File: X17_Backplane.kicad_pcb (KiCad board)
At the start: 2 copper layers, 89.2 x 110 mm, 30 parts, among them J1 430450212, J10 Conn_01x01, J11 Conn_01x01, J13 Conn_01x01, J14 ET60S-D04-3-08-D04-X-R1-S, J15 Conn_01x01, J16 Conn_01x01, J18 430450212, J19 DF11-10DS-2DSA05, J2 IPS1-105-01-L-D, J3 IPS1-105-01-L-D, J4 Conn_01x02_Pin, J5 Conn_01x04_Pin, J6 Conn_01x01, J7 Conn_01x01, J8 430450612, J9 Conn_01x01, U1 282837-4, U2 ULN2003AD, U3 SolenoidConn

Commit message: Work done on11/17/2024
I'm cooked yo
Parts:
- U1: value 282837-4 -> 282837-6; footprint TB_282837_4:282837-4_TYC -> 282837_6:282837-6_TYC
- moved J18 144.6 mm to (119.2, 146.5)
- moved J1 101.7 mm to (132.2, 146.5)
- moved U1 100.0 mm to (151.3, 145.8)
- moved J8 29.0 mm to (105.8, 146.5)
- moved J19 5.30 mm to (149.7, 131.8)
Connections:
- net A renamed A+
- net A_TB renamed A_TB+
- net B renamed A-
- J1 pad 1: B_TB -> A_TB-
- J14 pad 03: NRST2 -> NRST_PSB
- J14 pad 05: unconnected-(J14-Pad05) -> 48V
- J14 pad 06: unconnected-(J14-Pad06) -> 48V
- J14 pad 07: unconnected-(J14-Pad07) -> 48V_GND
- J14 pad 08: unconnected-(J14-Pad08) -> 48V_GND
- J14 pad P05_1: 48V_GND -> P05_7
- J14 pad P06_1: 48V_GND -> P06_6
- J14 pad P07_1: 48V -> P07_8
- J14 pad P08_1: 48V -> P08_6
- J19 pad 16: NRST -> NRST_ESCC
- J8 pad 3: 5V_TB -> NRST_PSB
- J8 pad 4: 5V_GNDTB -> NRST_ESCC
- J8 pad 5: NRST2 -> NRST_TB
- J8 pad 6: NRST -> 5V_GNDTB
- U1 pad 1: 48V -> 48V_GND
- U1 pad 2: 48V_GND -> 48V
- U1 pad 3: B_TB -> NRST_TB
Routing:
- net 12V_GND1: track 0.00 -> 153.8 mm, vias 0 -> 2
- net 12V_GND2: track 0.00 -> 130.9 mm, vias 0 -> 2
- net 5V: track 0.00 -> 130.5 mm
- net 48V: track 0.00 -> 72.6 mm
- net 48V_GND: track 0.00 -> 65.4 mm
- net A_TB+: track 0.00 -> 40.0 mm
- net A_TB-: track 0.00 -> 40.0 mm
- net A-: track 0.00 -> 36.9 mm, vias 0 -> 2
- net A+: track 0.00 -> 36.3 mm, vias 0 -> 2
- net 12V_1: track 0.00 -> 33.0 mm
- net 5V_GND: track 0.00 -> 21.4 mm, vias 0 -> 5
- net PWMB3: track 0.00 -> 11.6 mm
- net PWMB2: track 0.00 -> 9.69 mm
- net PWMB1: track 0.00 -> 8.95 mm
- net PWMB0: track 0.00 -> 8.68 mm
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- added copper zone on B.Cu, net 12V_1
- added copper zone on B.Cu, net 12V_2
- added copper zone on B.Cu, net 12V_GND1
- added copper zone on B.Cu, net 12V_GND2
- added copper zone on B.Cu, net 5V_GND
- removed copper zone on F.Cu, net 12V_1
- removed copper zone on F.Cu, net 12V_2
- removed copper zone on F.Cu, net 12V_GND1
- removed copper zone on F.Cu, net 12V_GND2

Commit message: WORK done on 11/20/2024
I'm losing my shiiiiiii
#SlayedTheDayAway
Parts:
- added R8: 4K, Resistor_SMD:R_0805_2012Metric, F.Cu at (264.2, 100.0)
- moved R6 131.1 mm to (126.8, 107.0), turned to -90 degrees
- moved R8 127.4 mm to (130.5, 128.2)
- moved D2 127.2 mm to (126.8, 102.0), turned to 90 degrees
- moved D4 126.0 mm to (127.2, 124.5)
- moved R5 111.6 mm to (151.5, 77.4), turned to -90 degrees
- moved D1 108.8 mm to (151.5, 73.2), turned to 90 degrees
- moved R7 94.7 mm to (168.5, 85.8), turned to -90 degrees
- moved D3 92.6 mm to (168.5, 80.8), turned to 90 degrees
- moved C2 64.0 mm to (192.2, 104.8), turned to -90 degrees
- moved U3 50.9 mm to (167.8, 62.0), turned to 90 degrees
- moved U2 31.7 mm to (154.9, 51.6), turned to 0 degrees
- moved J19 2.30 mm to (149.2, 129.5)
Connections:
- J19 pad 3: A+ -> PWMA1
- J19 pad 4: A- -> A+
- J19 pad 6: PWMA1 -> A-
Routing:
- net NRST_ESCC: track 0.00 -> 102.2 mm, vias 0 -> 6
- net NRST_PSB: track 0.00 -> 91.9 mm, vias 0 -> 4
- net 5V_GNDTB: track 0.00 -> 90.6 mm, vias 0 -> 8
- net 12V_2: track 0.00 -> 77.7 mm, vias 0 -> 14
- net A-: track 36.9 -> 114.0 mm, vias 2 -> 6
- net 12V_1: track 33.0 -> 110.1 mm, vias 0 -> 11
- net A+: track 36.3 -> 112.6 mm, vias 2 -> 4
- net PWMA3: track 0.00 -> 74.6 mm, vias 0 -> 2
- net NRST_TB: track 0.00 -> 74.5 mm, vias 0 -> 6
- net PWMA0: track 0.16 -> 70.8 mm
- net PWMA1: track 0.00 -> 64.5 mm
- net PWMA2: track 0.00 -> 60.4 mm, vias 0 -> 2
- net Telemetry: track 0.00 -> 58.7 mm, vias 0 -> 2
- net PWMB1: track 8.95 -> 59.3 mm, vias 0 -> 4
- net 12V_GND2: track 130.9 -> 88.2 mm, vias 2 -> 16
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- added copper zone on F.Cu, net 12V_1
- added copper zone on F.Cu, net 12V_2
- added copper zone on F.Cu, net 12V_GND1
- added copper zone on F.Cu, net 12V_GND2

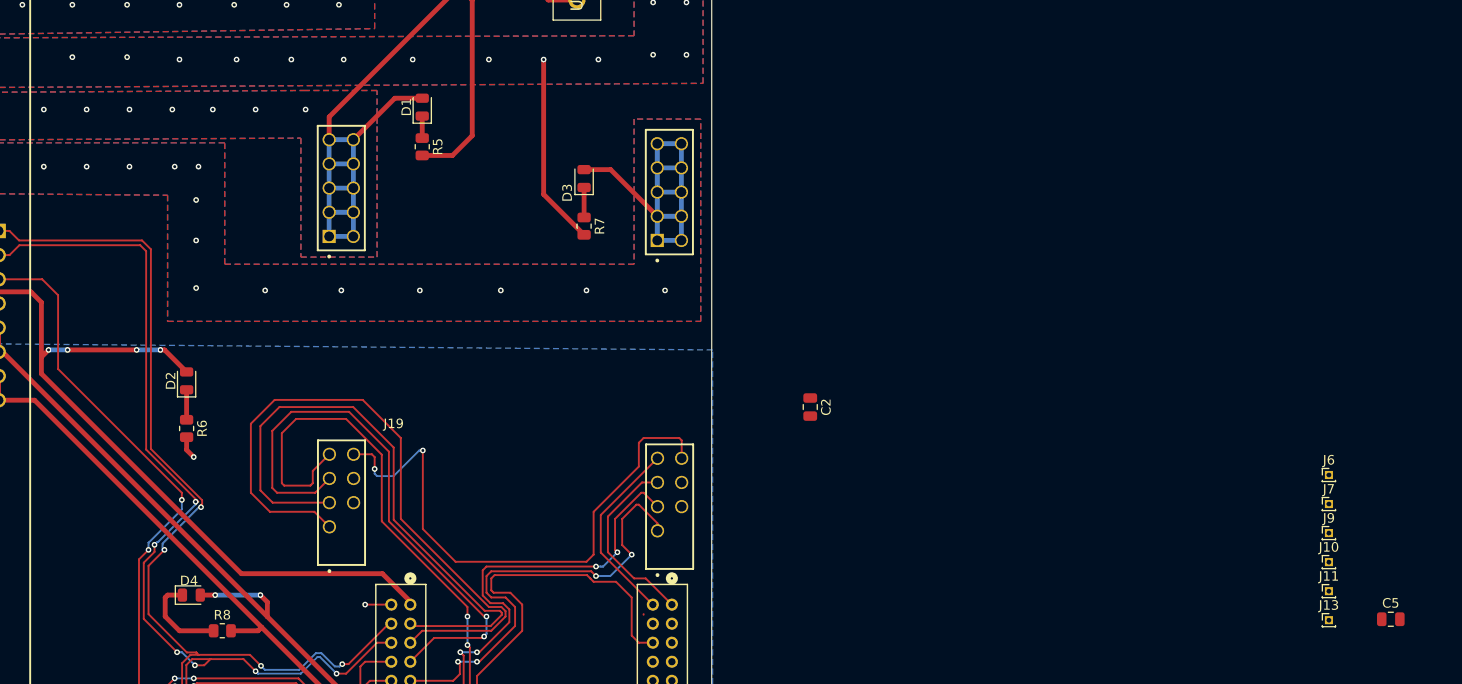
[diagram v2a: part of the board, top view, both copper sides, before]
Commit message: 11/20/2024
Yo fr tho Daniel and Vijay save my ass from these PCB demons
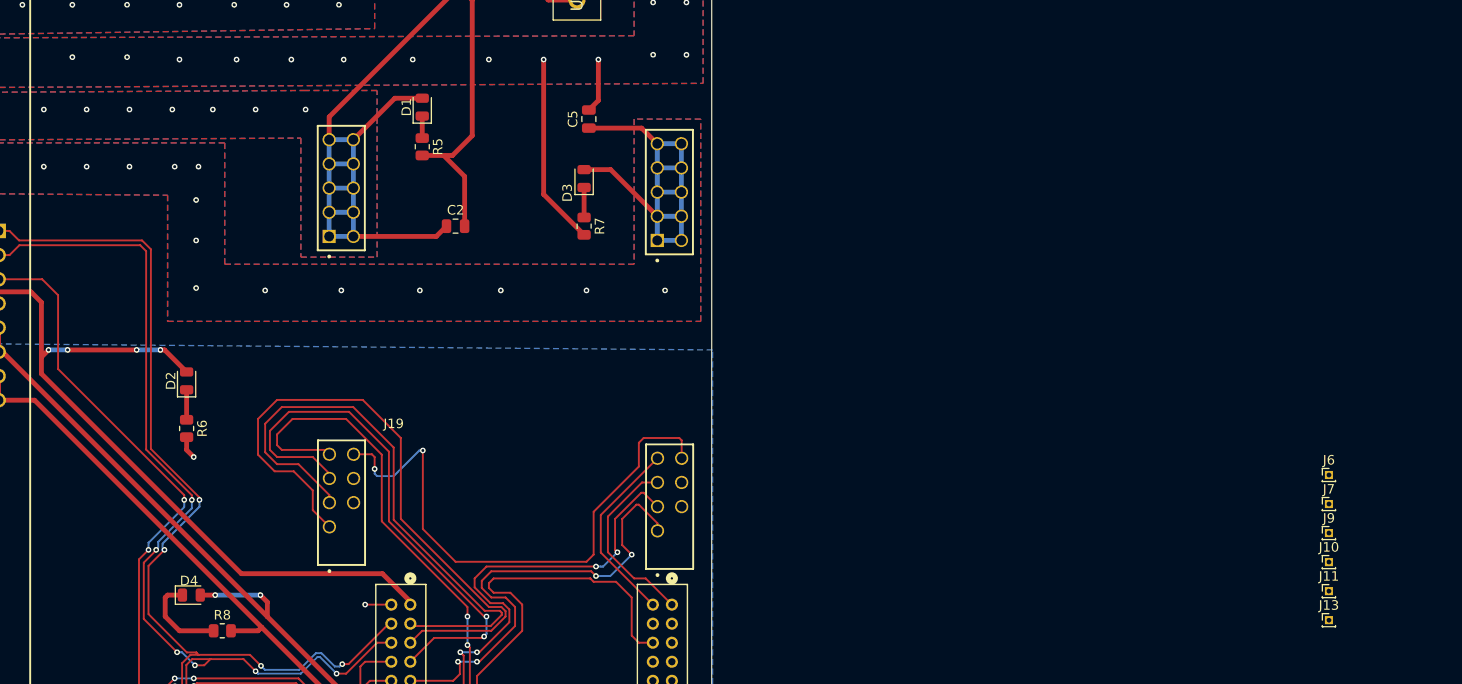
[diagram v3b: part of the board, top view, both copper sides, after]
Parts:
- moved C5 99.3 mm to (169.0, 74.5), turned to 90 degrees
- moved C2 41.8 mm to (155.0, 85.8), turned to 0 degrees
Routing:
- net 12V_1: track 110.1 -> 120.4 mm
- net 12V_GND1: track 136.6 -> 144.9 mm
- net 12V_2: track 77.7 -> 85.6 mm
- net 12V_GND2: track 88.2 -> 93.9 mm
- net PWMA3: track 74.6 -> 69.7 mm
- net PWMA2: track 60.4 -> 57.6 mm
- net PWMA1: track 64.5 -> 61.8 mm
- net PWMA0: track 70.8 -> 68.5 mm
- net A-: track 114.0 -> 113.2 mm
- net PWMB1: track 59.3 -> 60.0 mm

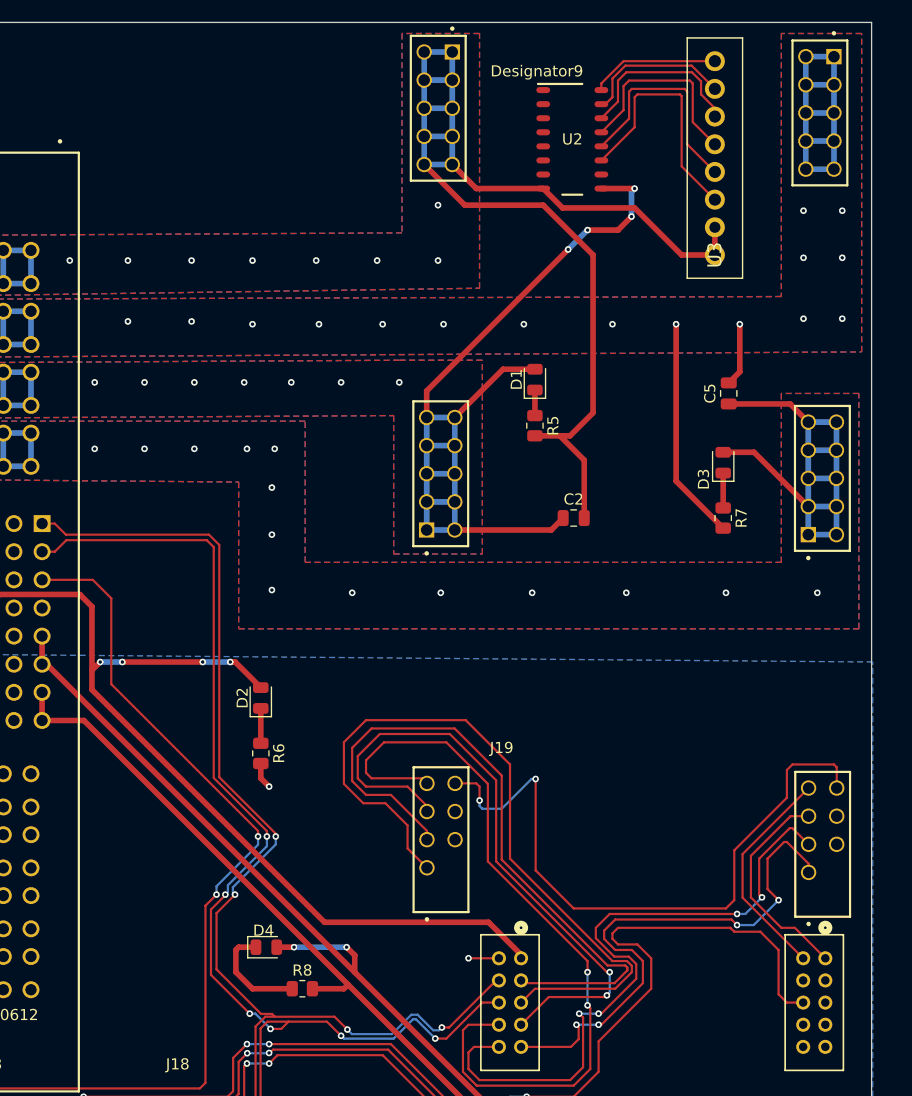
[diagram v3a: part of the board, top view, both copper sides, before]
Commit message: Work done on 11/21/2024
Made traces more size efficient(I think)
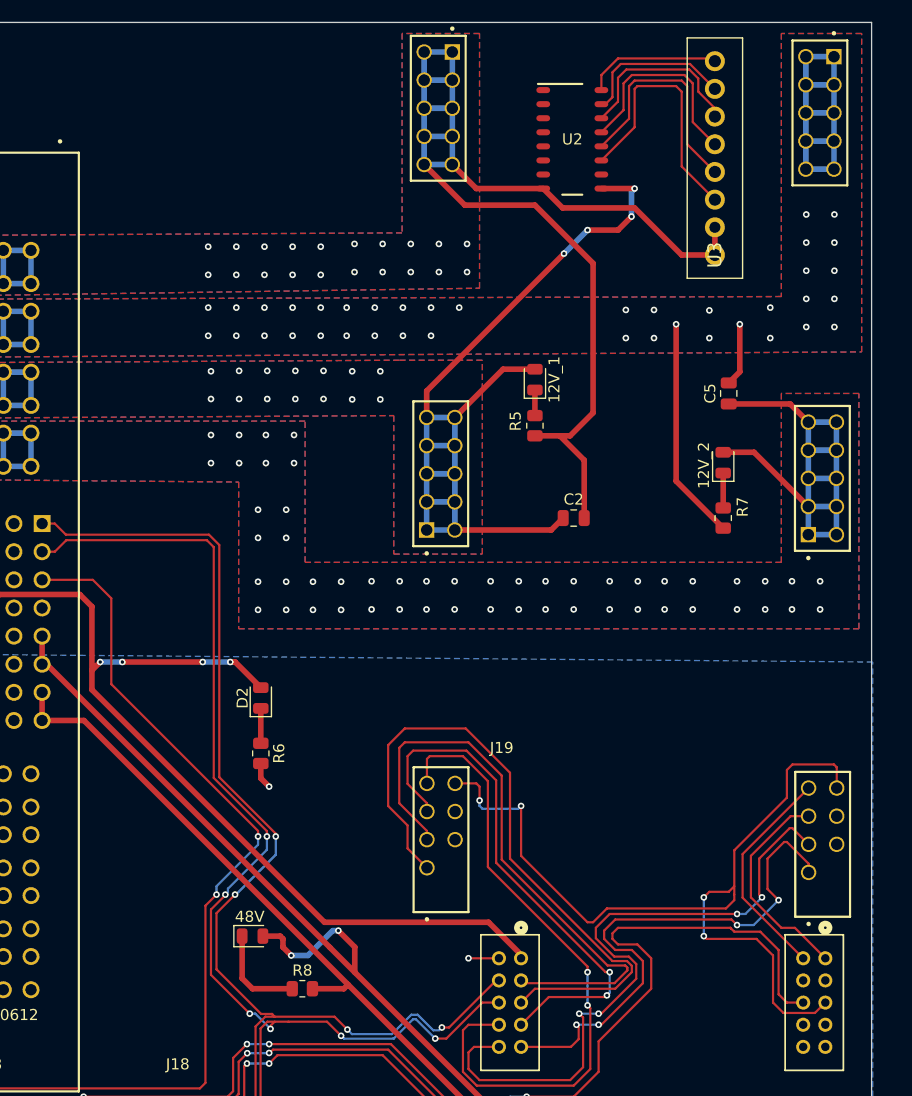
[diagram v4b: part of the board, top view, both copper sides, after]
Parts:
- moved 48V 1.60 mm to (126.0, 123.5)
- renumbered D1 to 12V_1, D3 to 12V_2, D4 to 48V
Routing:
- net Telemetry: track 58.7 -> 78.9 mm, vias 2 -> 4
- net PWMA3: track 69.7 -> 58.4 mm
- net PWMA2: track 57.6 -> 47.9 mm
- net PWMA1: track 61.8 -> 53.4 mm
- net PWMA0: track 68.5 -> 60.4 mm
- net 48V: track 81.5 -> 85.9 mm
- net SOL6_1: track 22.0 -> 23.3 mm
- net SOL5_1: track 19.7 -> 20.9 mm
- net A-: track 113.2 -> 112.1 mm
- net Net-(D4-K): track 9.62 -> 8.73 mm
- net SOL1_1: track 11.7 -> 12.3 mm
- net SOL4_1: track 17.9 -> 18.4 mm
- net 12V_GND1: track 144.9 -> 144.5 mm, vias 8 -> 20
- net 12V_GND2: vias 16 -> 39
- net 12V_2: vias 14 -> 52
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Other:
- board text added: "LED"

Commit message: Work done on 11/22/2024
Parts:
- removed the R8 at (264.2, 100.0)
- added J20: Conn_01x01, TestPoint:TestPoint_Pad_D4.0mm, F.Cu at (161.5, 135.2)
- added J21: Conn_01x01, TestPoint:TestPoint_Pad_D4.0mm, F.Cu at (170.2, 128.2)
- added J22: Conn_01x01, TestPoint:TestPoint_Pad_D4.0mm, F.Cu at (167.0, 135.2)
- added MOSI: Conn_01x01, TestPoint:TestPoint_Pad_D4.0mm, F.Cu at (165.0, 128.2)
- 12V_1: renamed from J7; footprint Connector_PinHeader_1.00mm:PinHeader_1x01_P1.00mm_Vertical -> TestPoint:TestPoint_Pad_D4.0mm
- 12V_2: renamed from J10; footprint Connector_PinHeader_1.00mm:PinHeader_1x01_P1.00mm_Vertical -> TestPoint:TestPoint_Pad_D4.0mm
- 12V_GND1: renamed from J9; footprint Connector_PinHeader_1.00mm:PinHeader_1x01_P1.00mm_Vertical -> TestPoint:TestPoint_Pad_D4.0mm
- 12V_GND2: renamed from J13; footprint Connector_PinHeader_1.00mm:PinHeader_1x01_P1.00mm_Vertical -> TestPoint:TestPoint_Pad_D4.0mm
- 48V: renamed from J6; footprint Connector_PinHeader_1.00mm:PinHeader_1x01_P1.00mm_Vertical -> TestPoint:TestPoint_Pad_D4.0mm
- 5V: renamed from J15; footprint Connector_PinHeader_1.00mm:PinHeader_1x01_P1.00mm_Vertical -> TestPoint:TestPoint_Pad_D4.0mm
- 5V_GND: renamed from J16; footprint Connector_PinHeader_1.00mm:PinHeader_1x01_P1.00mm_Vertical -> TestPoint:TestPoint_Pad_D4.0mm
- C2, C5: footprint Capacitor_SMD:C_0805_2012Metric -> EEE_FT1E561UPfootprints:CAP_FT_F_PAN
- J11: footprint Connector_PinHeader_1.00mm:PinHeader_1x01_P1.00mm_Vertical -> TestPoint:TestPoint_Pad_D4.0mm
- J2, J3: footprint ESCadapterfootprint:PWM, 12V, GND JST Connector (1) -> ESCadapterfootprint:PWM, 12V, GND JST Connector (real)
- J4: value Conn_01x02_Pin -> Conn_01x01; footprint Connector_PinHeader_1.00mm:PinHeader_1x02_P1.00mm_Vertical -> TestPoint:TestPoint_Pad_D4.0mm
- J5: value Conn_01x04_Pin -> Conn_01x01; footprint Connector_PinHeader_1.00mm:PinHeader_1x04_P1.00mm_Vertical -> TestPoint:TestPoint_Pad_D4.0mm
- R5, R6, R7, R8: footprint Resistor_SMD:R_0805_2012Metric -> Resistor_SMD:R_0603_1608Metric
- moved 12V_GND1 143.9 mm to (122.0, 46.2)
- moved 12V_GND2 124.2 mm to (141.0, 62.0)
- moved 12V_1 117.2 mm to (134.8, 80.5)
- moved 12V_2 117.0 mm to (134.8, 87.0)
- moved J11 100.4 mm to (149.0, 101.0)
- moved 48V 91.6 mm to (155.8, 101.5)
- moved J4 89.9 mm to (133.0, 107.2)
- moved 5V 82.0 mm to (137.0, 124.2)
- moved J5 75.4 mm to (133.5, 114.2)
- moved 5V_GND 67.3 mm to (142.5, 127.0)
- moved D3 6.88 mm to (170.8, 87.2), turned to 0 degrees
- moved D1 6.39 mm to (157.0, 76.5), turned to 0 degrees
- moved C5 2.61 mm to (168.2, 77.0)
- moved R7 2.50 mm to (166.5, 87.2), turned to 180 degrees
- moved J2 1.50 mm to (141.5, 82.0)
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- renumbered 12V_1 to D1, 12V_2 to D3, 48V to D4, J19 to SCLK
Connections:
- net P05_7 renamed P05_9
- net P06_6 renamed P06_7
- net P07_8 renamed P07_4
- net P08_6 renamed P08
- J5 pad 1: MISO -> A-
- U1 pad 1: 48V_GND -> NRST_TB
- U1 pad 2: 48V -> A_TB+
- U1 pad 3: NRST_TB -> A_TB-
- U1 pad 4: A_TB+ -> 48V_GND
- U1 pad 5: A_TB- -> 48V
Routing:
- net 48V: track 85.9 -> 150.4 mm, vias 2 -> 4
- net 48V_GND: track 68.7 -> 131.9 mm, vias 0 -> 4
- net SCLK: track 0.00 -> 26.0 mm
- net 12V_1: track 120.4 -> 143.6 mm, vias 18 -> 20
- net 12V_GND1: track 144.5 -> 164.5 mm, vias 20 -> 22
- net MISO: track 0.00 -> 15.4 mm
- net NRST_TB: track 74.5 -> 60.0 mm, vias 6 -> 4
- net MOSI: track 0.00 -> 12.1 mm
- net CS: track 0.00 -> 10.9 mm, vias 0 -> 2
- net A_TB-: track 43.5 -> 33.3 mm
- net A+: track 112.0 -> 121.7 mm
- net A-: track 112.1 -> 121.8 mm
- net A_TB+: track 41.7 -> 34.7 mm
- net 12V_2: track 85.6 -> 91.6 mm
- net 12V_GND2: track 93.9 -> 99.5 mm
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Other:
- board text added: "CS"
- board text added: "D1"

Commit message: Work done on 11/22/2024
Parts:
- moved 12V_1 0.56 mm to (135.2, 80.8)
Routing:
- net 12V_1: track 143.6 -> 149.7 mm
- net 12V_GND1: track 164.5 -> 165.5 mm
- net MISO: track 15.4 -> 16.0 mm
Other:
- board text added: "48VGND"
- board text added: "A+"
- board text added: "A-"
- board text added: "MISO"
- board text added: "SCLK"

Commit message: Work done on 11/23/2024
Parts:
- D1, D2, D3, D4: footprint LED_SMD:LED_0805_2012Metric -> LED_SMD:LED_0805_2012Metric_Pad1.15x1.40mm_HandSolder
- R5, R6, R7, R8: footprint Resistor_SMD:R_0603_1608Metric -> Resistor_SMD:R_0603_1608Metric_Pad0.98x0.95mm_HandSolder
- renumbered 12V_2 to J10, 12V_GND2 to J13, 5V to J15, 5V_GND to J16, SCLK to J19, MOSI to J23, 48V to J6, 12V_1 to J7, 12V_GND1 to J9

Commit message: Work done on 12/13/2024
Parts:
- removed C5: 180μF, EEE_FT1E561UPfootprints:CAP_FT_F_PAN
- removed D3: LED, LED_SMD:LED_0805_2012Metric_Pad1.15x1.40mm_HandSolder
- removed J10, J11, J13, J20, J21, J22, J23: Conn_01x01, TestPoint:TestPoint_Pad_D4.0mm
- removed R7: 600, Resistor_SMD:R_0603_1608Metric_Pad0.98x0.95mm_HandSolder
- added J4: Conn_01x04_Pin, Connector_PinHeader_2.54mm:PinHeader_1x04_P2.54mm_Vertical_SMD_Pin1Right, F.Cu at (108.9, 167.7)
- J6: value Conn_01x01 -> Conn_01x02_Pin; footprint TestPoint:TestPoint_Pad_D4.0mm -> Connector_PinHeader_2.54mm:PinHeader_1x02_P2.54mm_Vertical
- moved J6 82.8 mm to (74.0, 88.5)
- moved D2 68.6 mm to (68.0, 137.4)
- moved D4 68.6 mm to (67.3, 158.9)
- moved J15 68.6 mm to (78.3, 159.7)
- moved J16 68.6 mm to (83.8, 162.4)
- moved J4 68.6 mm to (74.3, 142.7)
- moved J5 68.6 mm to (74.8, 149.7)
- moved R6 68.6 mm to (68.0, 142.4)
- moved R8 68.6 mm to (71.8, 163.7)
- moved U3 26.2 mm to (166.8, 88.2)
- moved U2 26.2 mm to (153.9, 77.8)
- moved C2 25.8 mm to (129.6, 78.0), turned to 90 degrees
- moved J7 22.6 mm to (114.8, 71.2)
- moved J8 22.3 mm to (128.0, 146.5)
- moved J19 18.3 mm to (141.4, 113.0)
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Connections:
- C2 pad 1: 12V_1 -> 12V
- C2 pad 2: 12V_GND1 -> 12V_GND
- D1 pad 2: 12V_1 -> 12V
- J14 pad 05: 48V -> unconnected-(J14-Pad05)
- J14 pad 06: 48V -> unconnected-(J14-Pad06)
- J14 pad 07: 48V_GND -> unconnected-(J14-Pad07)
- J14 pad 08: 48V_GND -> unconnected-(J14-Pad08)
- J14 pad 19: unconnected-(J14-Pad19) -> 5V
- J14 pad 20: 5V -> 5V_GND
- J14 pad 21: 5V_GND -> 48V
- J14 pad 22: unconnected-(J14-Pad22) -> 48V
- J14 pad 23: unconnected-(J14-Pad23) -> 48V_GND
- J14 pad 24: unconnected-(J14-Pad24) -> 48V_GND
- J14 pad P01_1: 12V_GND1 -> P01_9
- J14 pad P02_1: 12V_GND2 -> P02_4
- J14 pad P03_1: 12V_1 -> P03_8
- J14 pad P04_1: 12V_2 -> P04_9
- J14 pad P05_1: P05_9 -> 12V
- J14 pad P08_1: P08 -> 12V_GND
- J2 pad 01: 12V_1 -> 12V
- J2 pad 03: 12V_GND1 -> 12V_GND
- J3 pad 01: 12V_2 -> 12V
- J3 pad 03: 12V_GND2 -> 12V_GND
- J6 pad 1: 48V -> A+
- J7 pad 1: 12V_1 -> 12V
- J9 pad 1: 12V_GND1 -> 12V_GND
- R5 pad 2: 12V_GND1 -> 12V_GND
- U2 pad 8: 12V_GND1 -> 12V_GND
- U2 pad 9: 12V_1 -> 12V
- U3 pad 1: 12V_GND1 -> 12V_GND
- U3 pad 2: 12V_GND1 -> 12V_GND
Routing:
- net 12V_GND1: track 165.5 -> 0.00 mm, vias 22 -> 0
- net 5V: track 163.3 -> 1.97 mm, vias 4 -> 0
- net 48V: track 150.4 -> 0.31 mm, vias 4 -> 0
- net 12V_1: track 149.7 -> 0.00 mm, vias 20 -> 0
- net 48V_GND: track 131.9 -> 0.00 mm, vias 4 -> 0
- net 12V: track 0.00 -> 126.8 mm, vias 0 -> 3
- net A+: track 121.7 -> 0.00 mm, vias 4 -> 0
- net A-: track 121.9 -> 1.20 mm, vias 6 -> 0
- net 12V_GND: track 0.00 -> 118.9 mm, vias 0 -> 3
- net NRST_ESCC: track 101.9 -> 0.00 mm, vias 6 -> 0
- net 12V_GND2: track 99.5 -> 0.00 mm, vias 39 -> 0
- net 12V_2: track 91.6 -> 0.00 mm, vias 52 -> 0
- net NRST_PSB: track 91.5 -> 0.00 mm, vias 4 -> 0
- net 5V_GNDTB: track 90.3 -> 0.00 mm, vias 8 -> 0
- net Telemetry: track 78.2 -> 0.00 mm, vias 4 -> 0
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- added copper zone on B.Cu, net 12V
- added copper zone on F.Cu, net 12V
- added copper zone on B.Cu, net 12V_GND
- added copper zone on F.Cu, net 12V_GND
- removed copper zone on B.Cu, net 12V_1
- removed copper zone on F.Cu, net 12V_1
- removed copper zone on B.Cu, net 12V_2
- removed copper zone on F.Cu, net 12V_2
- removed copper zone on B.Cu, net 12V_GND1
- removed copper zone on F.Cu, net 12V_GND1
- removed copper zone on B.Cu, net 12V_GND2
- removed copper zone on F.Cu, net 12V_GND2
- removed copper zone on B.Cu, net 5V_GND
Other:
- board text removed: "48VGND"
- board text removed: "CS"
- board text removed: "MISO"
- board text removed: "SCLK"
